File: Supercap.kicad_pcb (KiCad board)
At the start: 4 copper layers, 151.8 x 70 mm, 69 parts, among them IC1 NCP5109ADR2G, IC2 NCP5109ADR2G, J1 XT30, J2 XT30, J2-J1 Conn_01x10, J3 Conn_01x01, J3-J1 Conn_01x10, J4 Conn_01x01, P7803B-1000R1 P7803B-1000, P7812B-1000R1 490-P7812B-1000, U1 TLV2372, U2 TLV2372, U4 ACS71240KEXBLT-010B3, U6 LP-MSPM0G3507

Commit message: laid out PCB rev C
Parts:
- added C_{filter}1: 10u, Capacitor_SMD:C_0603_1608Metric_Pad1.08x0.95mm_HandSolder, F.Cu at (145.2, 130.4)
- added R_{filter}1: 3.3, Resistor_SMD:R_0603_1608Metric_Pad0.98x0.95mm_HandSolder, F.Cu at (148.5, 130.4)
- C_{RC}1: renamed from C_{RC}2; moved to F.Cu
- C_{RC}2: renamed from C_{RC}1; moved to F.Cu
- C_{byp}1: renamed from C_{byp}2; moved to B.Cu
- C_{d1}1, C_{d2}1, C_{d3}1, C_{d4}1, C_{d5}1, C_{d6}1, P7812B-1000R1, R1, R2, R3, R4, R_{sens,bottom}2, R_{sens,top}1, R_{sens,top}2, U1, U2: moved to F.Cu
- C_{l}1: renamed from C_{l}2; moved to B.Cu
- C_{smooth}2: renamed from C_{smooth}1; moved to F.Cu
- C_{smooth}3: renamed from C_{smooth}2; moved to B.Cu
- C_{smooth}4: renamed from C_{smooth}6; moved to F.Cu
- C_{smooth}5: renamed from C_{smooth}7; moved to F.Cu
- J2: renamed from J4; moved to B.Cu
- J4: renamed from J1; moved to F.Cu
- R_{RC}1: renamed from R_{RC}2; moved to B.Cu
- R_{RC}2: renamed from R_{RC}1; moved to B.Cu
- R_{pu}1: renamed from R_{pu}2; moved to B.Cu
- R_{sens,bottom}1: moved to B.Cu
- U3: renamed from U4; moved to F.Cu
- moved U4 91.5 mm to (110.3, 66.9), turned to 90 degrees
- moved GNDPWR1 79.2 mm to (157.8, 137.3), turned to 0 degrees
- moved C_{smooth}2 77.9 mm to (99.3, 131.3)
- moved R4 71.7 mm to (102.4, 139.8), turned to 180 degrees
- moved U1 71.0 mm to (102.8, 133.3)
- moved Q_{bottom,1}2 70.4 mm to (130.1, 160.0), turned to -90 degrees
- moved R3 69.9 mm to (103.3, 138.1), turned to 0 degrees
- moved C_{d4}1 68.1 mm to (145.7, 163.2), turned to 0 degrees
- moved J2-J1 67.4 mm to (123.7, 157.8), turned to 90 degrees
- moved R_{small,bottom}2 66.0 mm to (130.4, 155.4)
- moved C_{d5}1 65.0 mm to (145.7, 160.0), turned to 0 degrees
- moved R2 64.5 mm to (102.3, 142.5), turned to 90 degrees
- moved R1 64.4 mm to (104.1, 142.5), turned to 90 degrees
- moved C_{d6}1 62.7 mm to (145.7, 156.8), turned to 0 degrees
- moved C_{bulk,out}1 60.7 mm to (150.8, 155.3), turned to -90 degrees
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- renumbered C_{smooth}3 to C_{smooth}1, J3 to J1, J2 to J3, U6 to U4
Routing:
- net /Control/PA22: track 92.8 -> 18.1 mm, vias 4 -> 2
- net /Control/PA8: track 92.1 -> 20.2 mm, vias 1 -> 2
- net /Control/I_{bat,out+}: track 0.00 -> 65.9 mm, vias 34 -> 33
- net /Control/+3V3: track 42.9 -> 100.1 mm, vias 6 -> 3
- net /Control/F_bat: track 25.3 -> 74.5 mm, vias 2 -> 1
- net /Voltage Converter/V_{sw,2}: track 7.37 -> 48.1 mm, vias 9 -> 40
- net /Control/I_bat: track 28.0 -> 66.8 mm
- net /Control/PB9: track 72.6 -> 41.6 mm, vias 2 -> 1
- net /Voltage Converter/HI_DRV_{1}: track 23.1 -> 54.0 mm, vias 0 -> 1
- net /Control/V_{bat,sens}: track 2.09 -> 30.7 mm
- net /Housekeeping/+12V: track 32.0 -> 55.9 mm, vias 2 -> 3
- net /Control/PA25: track 80.3 -> 57.8 mm
- net /Voltage Converter/V_{sw,1}: track 25.7 -> 44.4 mm, vias 1 -> 2
- net /Voltage Converter/LO_DRV_{1}: track 36.0 -> 53.8 mm
- net /Control/V_{sc,sens}: track 4.24 -> 21.1 mm, vias 1 -> 2
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- added copper zone on B.Cu, net /Control/+3V3
- added copper zone on B.Cu, net /Housekeeping/MiniPC
- added copper zone on F.Cu, net /Housekeeping/MiniPC
- added copper zone on In1.Cu, net /Housekeeping/MiniPC
- added copper zone on In2.Cu, net /Housekeeping/MiniPC
- added copper zone on In1.Cu, net GND
- removed copper zone on In1.Cu, net /Control/+3V3
- removed copper zone on In1.Cu, net /Voltage Converter/V_{sw,1}
- removed copper zone on In2.Cu, net /Voltage Converter/V_{sw,1}
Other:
- board size 151.8 x 70 mm -> 139 x 70 mm
- board text added: "Power Inductor Size"

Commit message: finished prelim board layout pending filter inductor redesign
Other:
- board text added: "Filter Inductor Size"
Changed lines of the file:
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@@
+	)
+	(gr_rect
+		(start 134.75 103)
+		(end 154.75 123)
+		(stroke
+			(width 0.1)
+			(type default)
+		)
+		(fill no)
+		(layer "Cmts.User")
 	)
 	(gr_rect
@@
 		(layer "Cmts.User")
 		(effects
+			(font
+				(size 1 1)
+				(thickness 0.15)
+			)
+			(justify left bottom)
+		)
+	)
+	(gr_text "Filter Inductor Size"
+		(at 134.75 104.5 0)
+		(layer "Cmts.User")
+		(effects

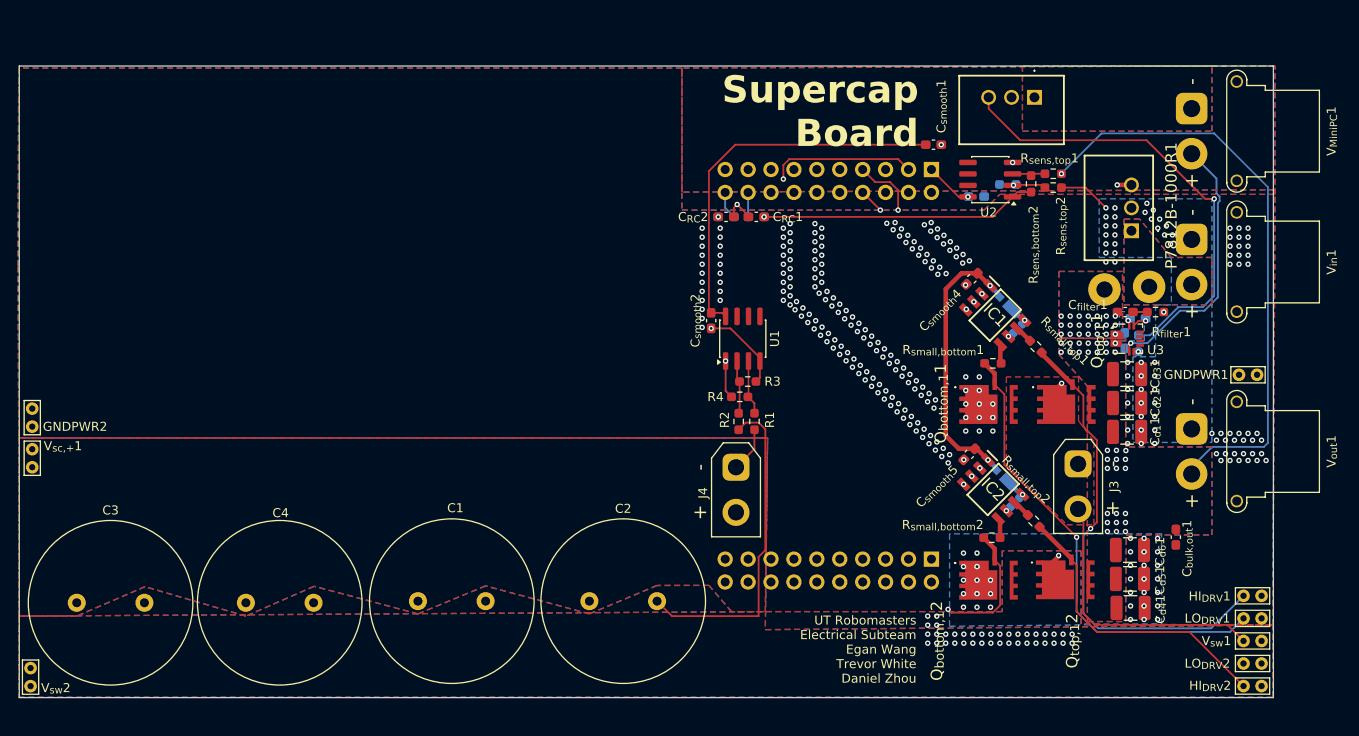
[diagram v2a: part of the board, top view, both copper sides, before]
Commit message: added parallel capacitance, minor cleanup to design - jed review + approval
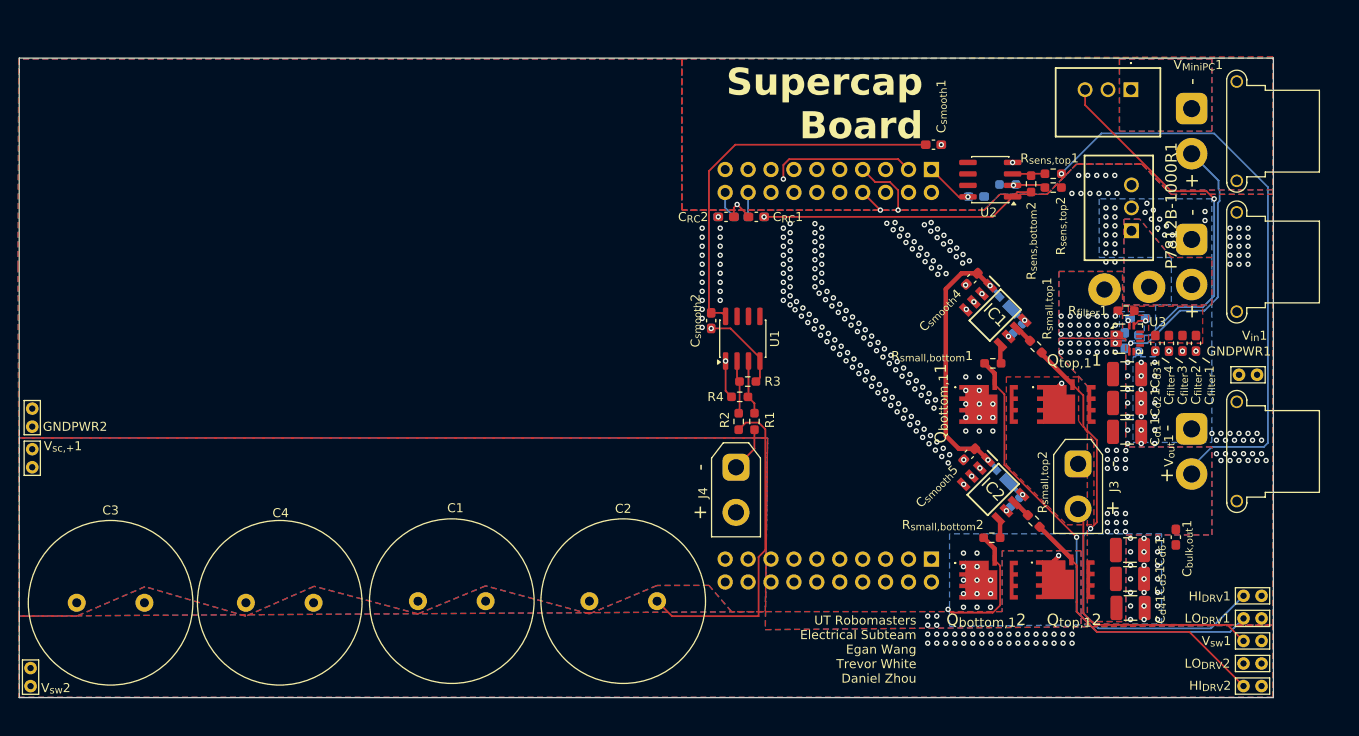
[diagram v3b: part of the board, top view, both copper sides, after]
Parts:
- added C_{filter}2: 10u, Capacitor_SMD:C_0603_1608Metric_Pad1.08x0.95mm_HandSolder, F.Cu at (151.5, 133.9)
- added C_{filter}3: 10u, Capacitor_SMD:C_0603_1608Metric_Pad1.08x0.95mm_HandSolder, F.Cu at (150.0, 133.9)
- added C_{filter}4: 10u, Capacitor_SMD:C_0603_1608Metric_Pad1.08x0.95mm_HandSolder, F.Cu at (148.5, 133.9)
- moved P7803B-1000R1 10.7 mm to (145.8, 105.8)
- moved C_{filter}1 8.57 mm to (153.0, 133.9), turned to -90 degrees
- moved R_{filter}1 3.27 mm to (145.2, 130.2)
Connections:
- C_{filter}1 pad 1: Net-(J2-Pin_1) -> Net-(C_{filter}1-Pad1)
- C_{filter}1 pad 2: Net-(C_{filter}1-Pad2) -> GNDPWR
- R_{filter}1 pad 1: Net-(C_{filter}1-Pad2) -> Net-(J2-Pin_1)
- R_{filter}1 pad 2: GNDPWR -> Net-(C_{filter}1-Pad1)
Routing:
- net /Control/+3V3: track 100.1 -> 90.0 mm
- net GNDPWR: track 5.86 -> 0.00 mm, vias 310 -> 326
- net Net-(C_{filter}1-Pad2): track 1.59 -> 0.00 mm
- net /Housekeeping/+12V: vias 3 -> 2
- added copper zone on F.Cu, net Net-(C_{filter}1-Pad1)
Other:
- board size 139 x 70 mm -> 139 x 70.9 mm

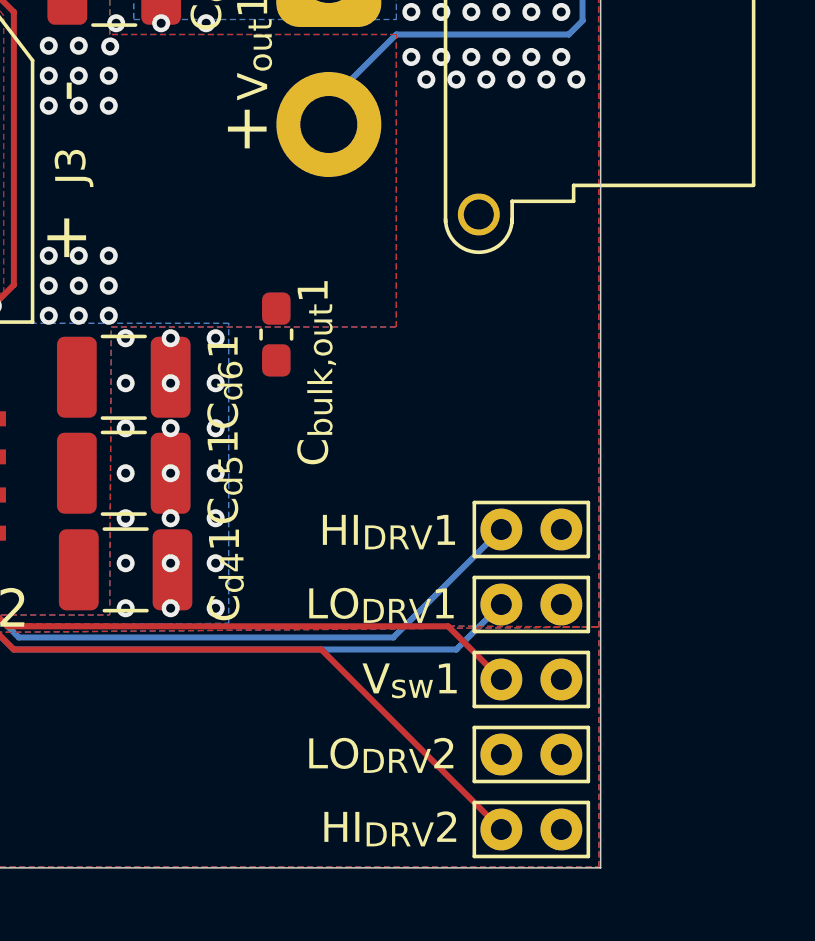
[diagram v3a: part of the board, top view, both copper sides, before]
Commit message: added heatsinks + more bulk capacitance footprints
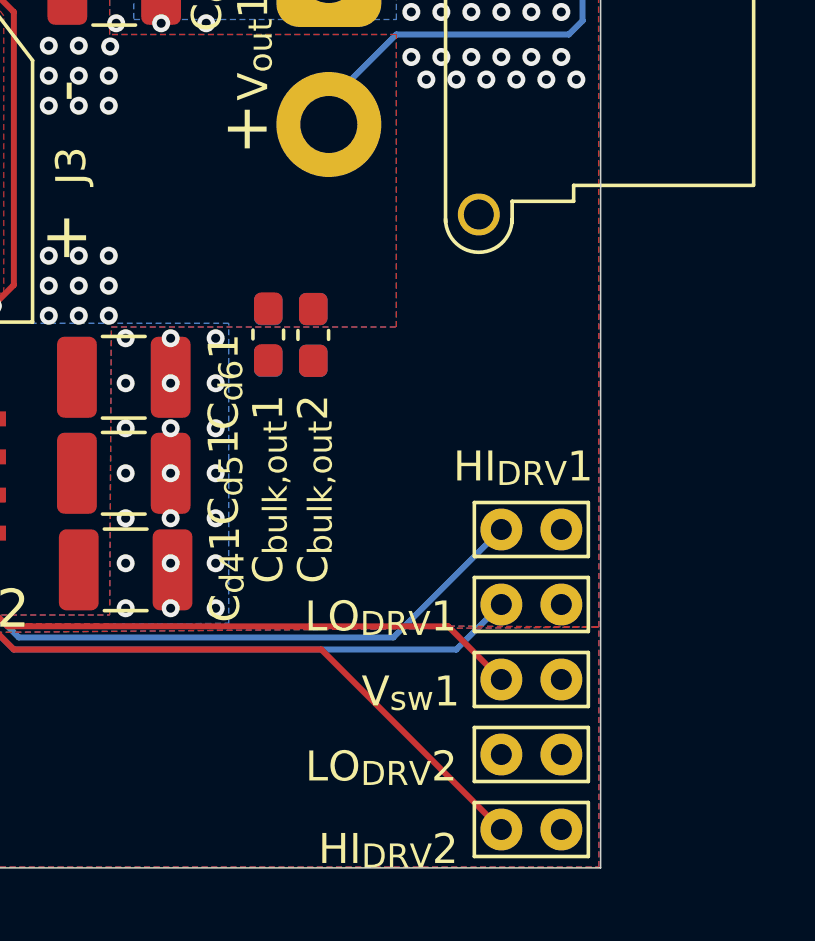
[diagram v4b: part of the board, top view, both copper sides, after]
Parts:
- added C_{bulk,out}2: ~, Capacitor_SMD:C_0603_1608Metric_Pad1.08x0.95mm_HandSolder, F.Cu at (152.0, 155.4)
- added C_{bulk,out}3: ~, Capacitor_SMD:C_0603_1608Metric_Pad1.08x0.95mm_HandSolder, B.Cu at (150.5, 155.4)
- added C_{bulk,out}4: ~, Capacitor_SMD:C_0603_1608Metric_Pad1.08x0.95mm_HandSolder, B.Cu at (152.0, 155.4)
- moved C_{bulk,out}1 0.27 mm to (150.5, 155.3)

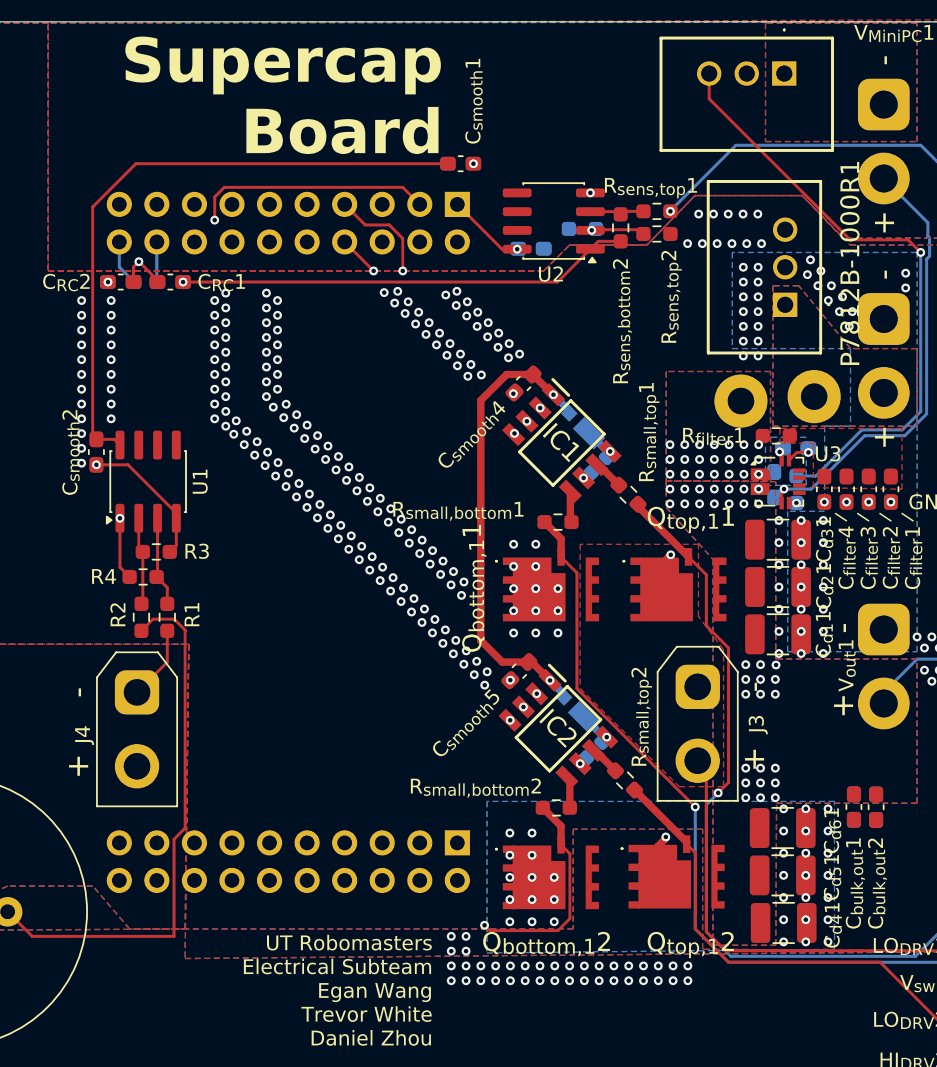
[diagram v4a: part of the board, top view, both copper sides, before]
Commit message: added better smoothing behavior to power supplies and op-amps as per application notes, switched resistors to op-amp with higher values
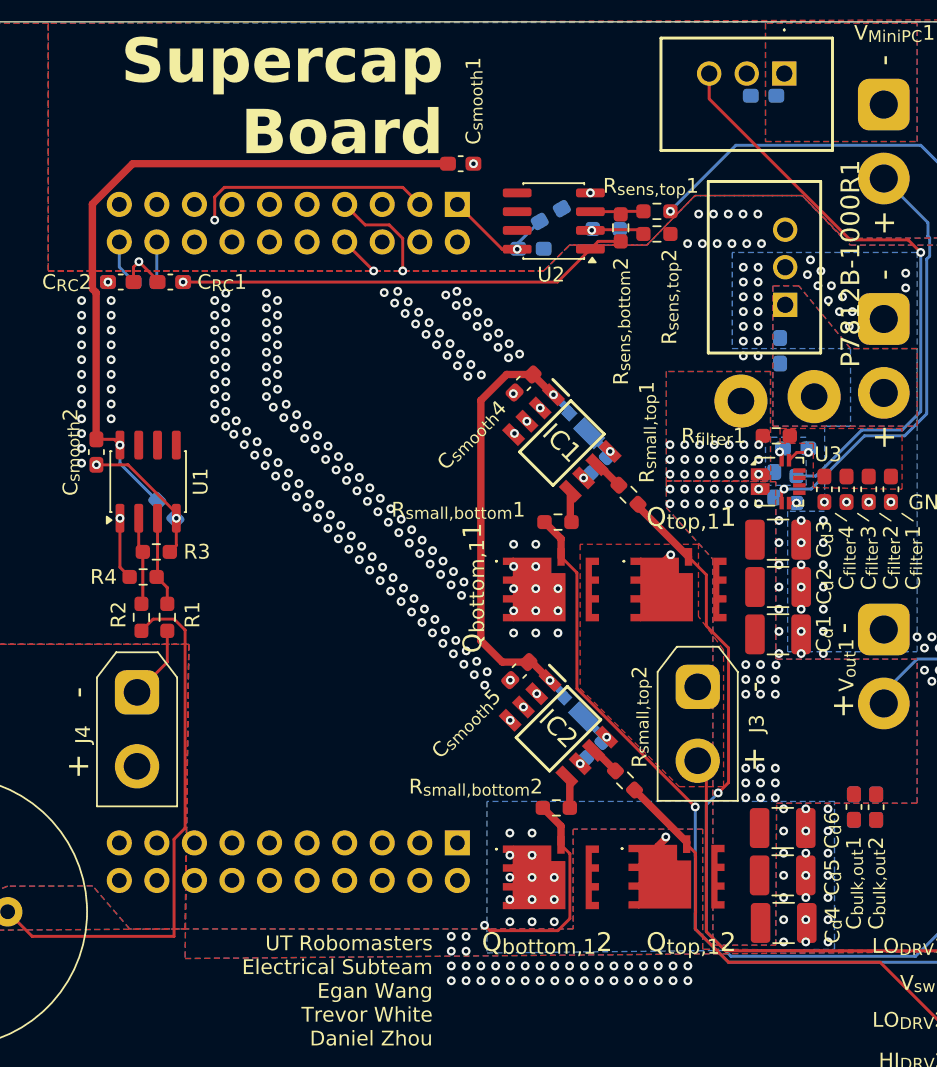
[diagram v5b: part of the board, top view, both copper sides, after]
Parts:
- added C_{d}7: 0.1u, Capacitor_SMD:C_0603_1608Metric_Pad1.08x0.95mm_HandSolder, B.Cu at (104.0, 135.2)
- added C_{d}8: 0.1u, Capacitor_SMD:C_0603_1608Metric_Pad1.08x0.95mm_HandSolder, B.Cu at (130.0, 115.3)
- added C_{smooth}6: 4.7u, Capacitor_SMD:C_0603_1608Metric_Pad1.08x0.95mm_HandSolder, B.Cu at (144.4, 107.2)
- added C_{smooth}7: 4.7u, Capacitor_SMD:C_0603_1608Metric_Pad1.08x0.95mm_HandSolder, B.Cu at (145.5, 124.5)
- R1, R2: value 1000 -> 10k
- R3, R4: value 1100 -> 11k
- moved R_{sens,bottom}1 1.61 mm to (133.8, 116.3), turned to 180 degrees
- renumbered C_{d1}1 to C_{d}1, C_{d2}1 to C_{d}2, C_{d3}1 to C_{d}3, C_{d4}1 to C_{d}4, C_{d5}1 to C_{d}5, C_{d6}1 to C_{d}6
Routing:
- net /Control/+3V3: track 90.0 -> 97.4 mm, vias 3 -> 4
- net GND: vias 5 -> 6
